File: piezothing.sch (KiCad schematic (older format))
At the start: 5 parts, among them J1 con, Y1 Piezo, Y2 Piezo

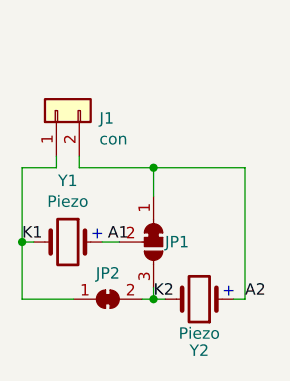
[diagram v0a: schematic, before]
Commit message: Added second connector, fixed ring short
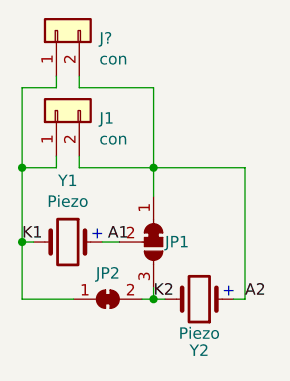
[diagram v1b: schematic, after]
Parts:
- added J?: con, Connector_PinHeader_2.54mm:PinHeader_1x02_P2.54mm_Horizontal, symbol Connector_Generic:Conn_01x02
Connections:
- net A2: now also J?.2 (Pin_2)
- net K1: now also J?.1 (Pin_1)
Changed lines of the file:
@@
 EESchema Schematic File Version 4
+LIBS:piezothing-cache
 EELAYER 26 0
 EELAYER END
@@
 Wire Wire Line
 	5300 2450 5375 2450
+$Comp
+L Connector_Generic:Conn_01x02 J?
+U 1 1 5C75539A
+P 5100 1525
+F 0 "J?" V 5066 1337 50  0000 R CNN
+F 1 "con" V 4975 1337 50  0000 R CNN
+F 2 "Connector_PinHeader_2.54mm:PinHeader_1x02_P2.54mm_Horizontal" H 5100 1525 50  0001 C CNN
+F 3 "~" H 5100 1525 50  0001 C CNN
+	1    5100 1525
+	0    -1   -1   0
+$EndComp
+Wire Wire Line
+	5100 1725 5100 1775
+Wire Wire Line
+	5100 1775 4950 1775
+Wire Wire Line
+	4950 1775 4950 2125
+Connection ~ 4950 2125
+Wire Wire Line
+	5200 1725 5200 1775
+Wire Wire Line
+	5200 1775 5525 1775
+Wire Wire Line
+	5525 1775 5525 2125
 $EndSCHEMATC
